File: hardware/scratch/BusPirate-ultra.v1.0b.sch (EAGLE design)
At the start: 174 parts, among them IC1 23LC1024, IC10 SN74LVC1T45DBV, IC11 SN74LVC1T45DBV, IC12 74LVC1G07DBV, IC13 SN74LVC1T45DBV, IC17 74LVC1G07DBV, IC18 SN74LVC1T45DBV, IC19 74LVC1G07DBV, IC2 23LC1024, IC20 SN74LVC1T45DBV, IC21 74LVC1G07DBV, IC22 SN74LVC1T45DBV, IC23 MCP1824_ADJ, IC24 74HCT4051, IC4 74LVC1G07DBV, IC5 74LVC1G07DBV, IC6 74LVC1G07DBV, IC7 74LVC1G07DBV, IC8 SN74LVC1T45DBV, IC9 SN74LVC1T45DBV, J2 CON_HEADER_1X04, J4 CON_HEADER_1X10-RIGHT_ANGLED_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, Q1 DMMT3906W, U1 W25X40CL, U2 STM32F103ZX, U3 ICE40HX4K, U4 MCP6001, U5 74LVC245A, U7 MCP6001, U8 74HCT4066PW, U9 74HCT4066PW

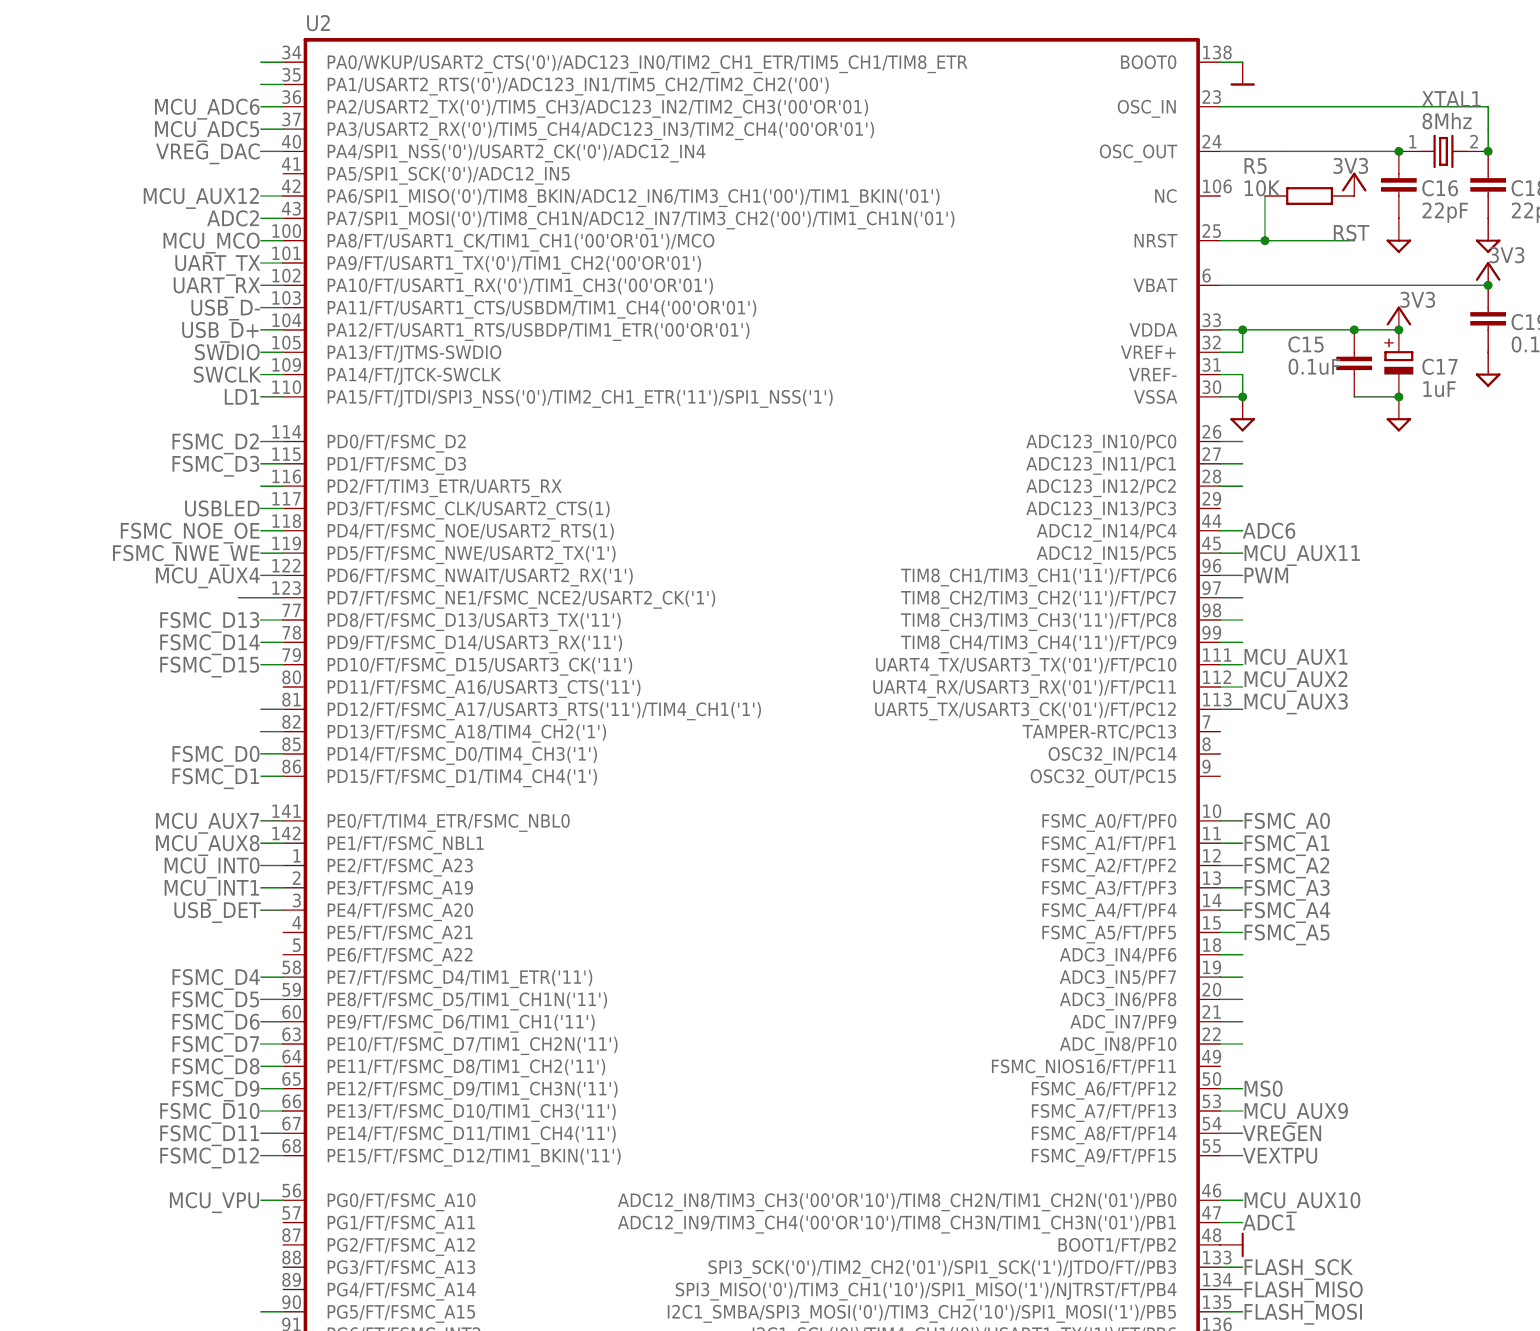
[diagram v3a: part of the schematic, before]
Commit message: move MCU_AUX12 to pin 55, reserve MCU 41-43 pins for display
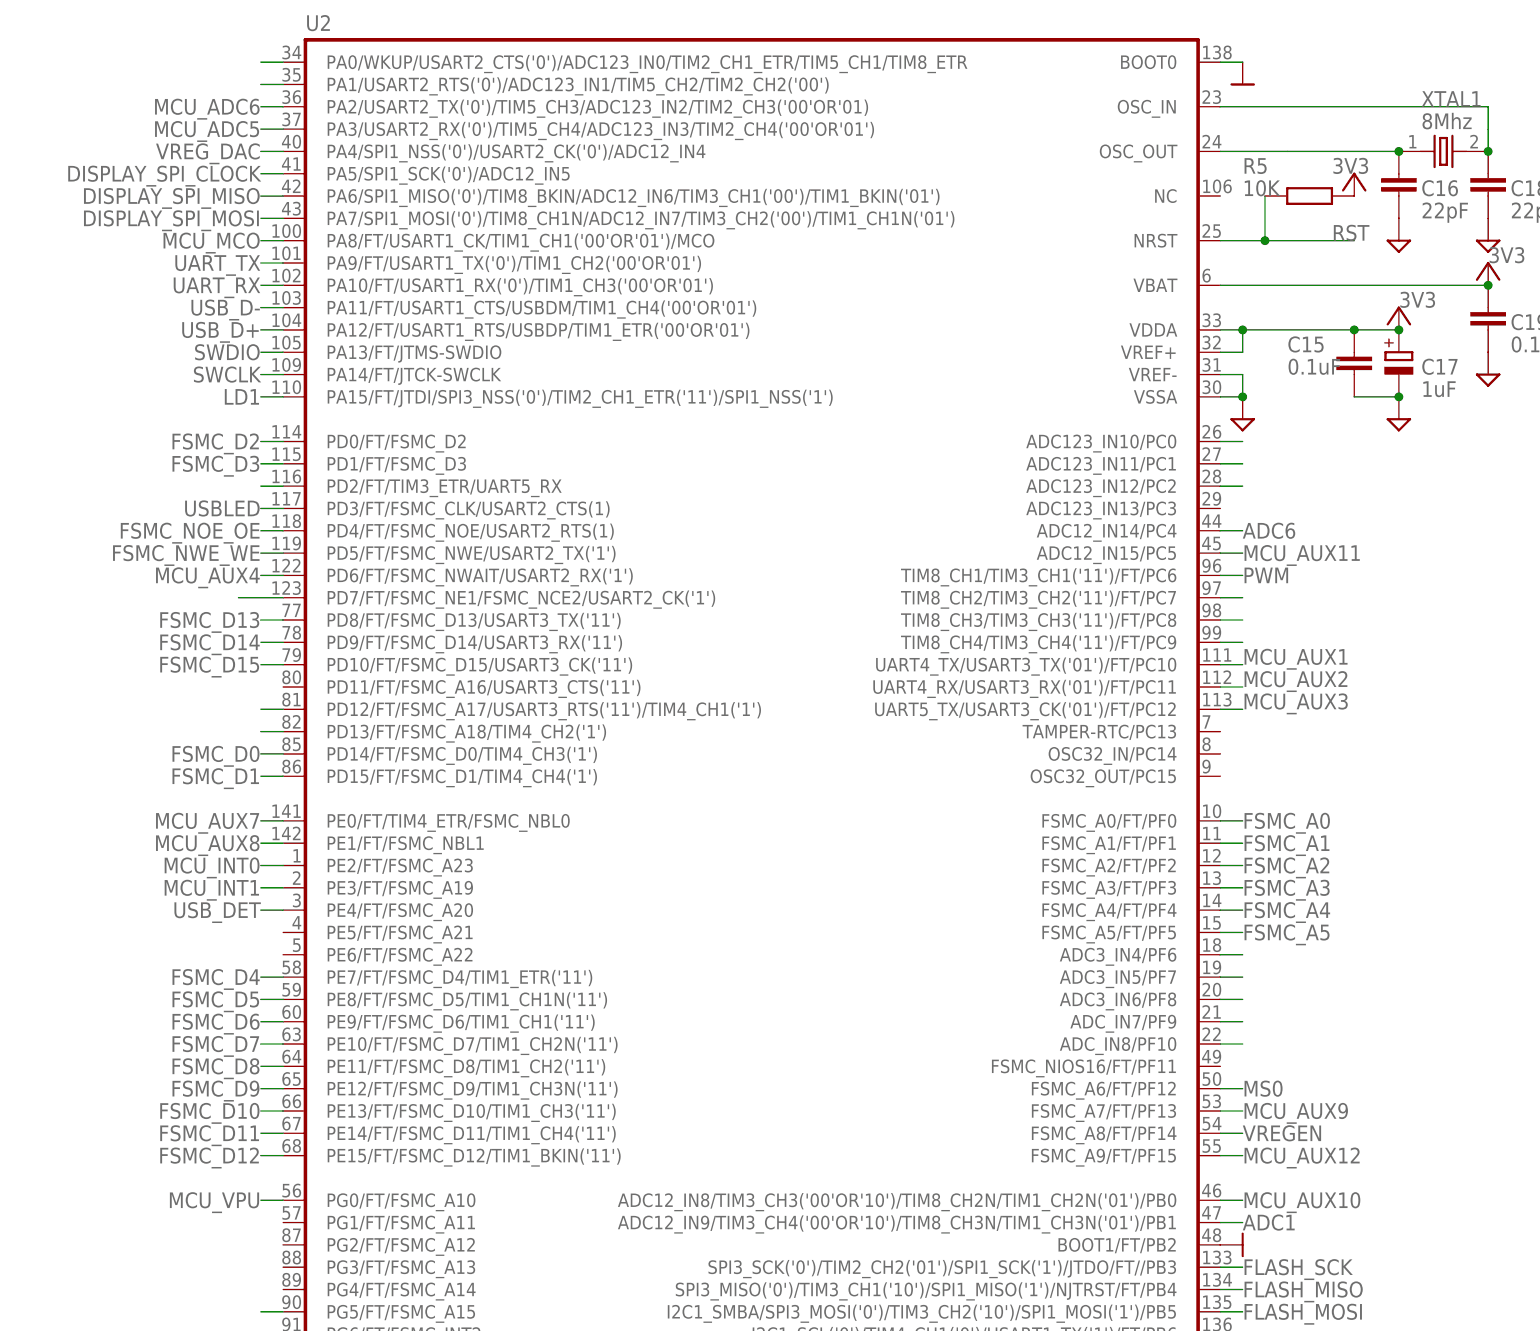
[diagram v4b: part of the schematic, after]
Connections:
- net ADC2 renamed DISPLAY_SPI_MOSI
- removed net VEXTPU: U2U.FSMC_A9/FT/PF15
- new net DISPLAY_SPI_CLOCK: U2U.PA5/SPI1_SCK('0')/ADC12_IN5
- new net DISPLAY_SPI_MISO: U2U.PA6/SPI1_MISO('0')/TIM8_BKIN/ADC12_IN6/TIM3_CH1('00')/TIM1_BKIN('01')
- net MCU_AUX12: now also U2U.FSMC_A9/FT/PF15; no longer U2U.PA6/SPI1_MISO('0')/TIM8_BKIN/ADC12_IN6/TIM3_CH1('00')/TIM1_BKIN('01')
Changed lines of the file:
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@@
-</segment>
-</net>
-<net name="ADC2" class="0">
-<segment>
-<pinref part="U2" gate="U" pin="PA7/SPI1_MOSI('0')/TIM8_CH1N/ADC12_IN7/TIM3_CH2('00')/TIM1_CH1N('01')"/>
-<wire x1="38.1" y1="411.48" x2="35.56" y2="411.48" width="0.1524" layer="91"/>
-<label x="35.56" y="411.48" size="1.778" layer="95" align="center-right"/>
 </segment>
 </net>
@@
 </segment>
 </net>
-<net name="VEXTPU" class="0">
-<segment>
-<pinref part="U2" gate="U" pin="FSMC_A9/FT/PF15"/>
-<wire x1="144.78" y1="304.8" x2="147.32" y2="304.8" width="0.1524" layer="91"/>
-<label x="147.32" y="304.8" size="1.778" layer="95" align="center-left"/>
-</segment>
-</net>
 <net name="UART_RX" class="0">
 <segment>
@@
 </segment>
 <segment>
-<pinref part="U2" gate="U" pin="PA6/SPI1_MISO('0')/TIM8_BKIN/ADC12_IN6/TIM3_CH1('00')/TIM1_BKIN('01')"/>
-<wire x1="38.1" y1="414.02" x2="35.56" y2="414.02" width="0.1524" layer="91"/>
-<label x="35.56" y="414.02" size="1.778" layer="95" align="center-right"/>
+<pinref part="U2" gate="U" pin="FSMC_A9/FT/PF15"/>
+<wire x1="144.78" y1="304.8" x2="147.32" y2="304.8" width="0.1524" layer="91"/>
+<label x="147.32" y="304.8" size="1.778" layer="95" align="center-left"/>
 </segment>
 </net>
@@
 </segment>
 </net>
+<net name="DISPLAY_SPI_CLOCK" class="0">
+<segment>
+<pinref part="U2" gate="U" pin="PA5/SPI1_SCK('0')/ADC12_IN5"/>
+<wire x1="38.1" y1="416.56" x2="35.56" y2="416.56" width="0.1524" layer="91"/>
+<label x="35.56" y="416.56" size="1.778" layer="95" align="center-right"/>
+</segment>
+</net>
+<net name="DISPLAY_SPI_MOSI" class="0">
+<segment>
+<pinref part="U2" gate="U" pin="PA7/SPI1_MOSI('0')/TIM8_CH1N/ADC12_IN7/TIM3_CH2('00')/TIM1_CH1N('01')"/>
+<wire x1="38.1" y1="411.48" x2="35.56" y2="411.48" width="0.1524" layer="91"/>
+<label x="35.56" y="411.48" size="1.778" layer="95" align="center-right"/>
+</segment>
+</net>
+<net name="DISPLAY_SPI_MISO" class="0">
+<segment>
+<pinref part="U2" gate="U" pin="PA6/SPI1_MISO('0')/TIM8_BKIN/ADC12_IN6/TIM3_CH1('00')/TIM1_BKIN('01')"/>
+<wire x1="38.1" y1="414.02" x2="35.56" y2="414.02" width="0.1524" layer="91"/>
+<label x="35.56" y="414.02" size="1.778" layer="95" align="center-right"/>
+</segment>
+</net>

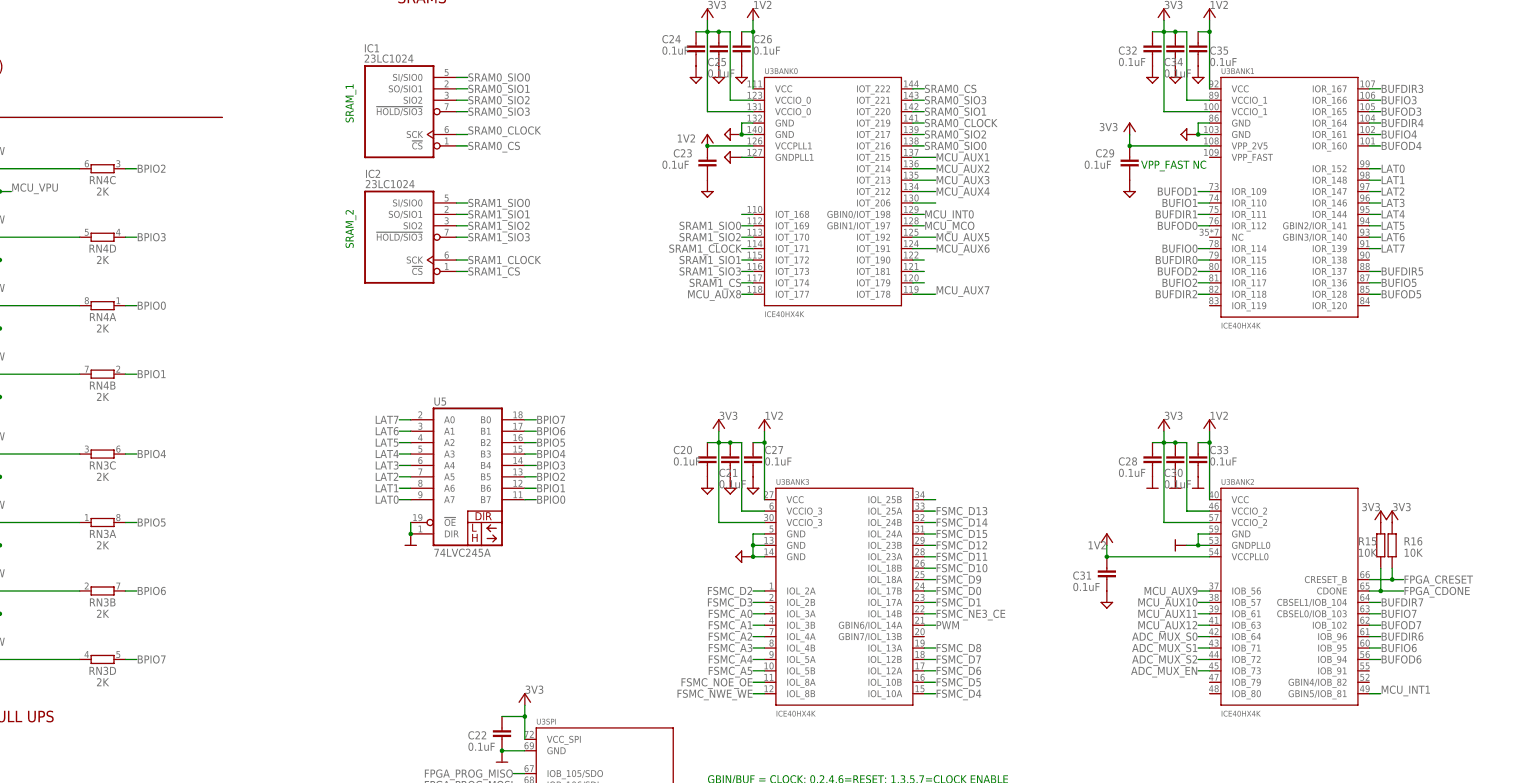
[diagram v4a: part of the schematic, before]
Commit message: changes in FPGA pin connection *BANK 1
BUFOD0 102
BUFIO0 104
BUFDIR0 101

BUFOD1 106
BUFIO1 107
BUFDIR1 105

BUFOD2 95
BUFIO2 96
BUFDIR2 94

BUFOD3 98
BUFIO3 99
BUFDIR3 97

BUFOD4 80
BUFIO4 81
BUFDIR4 82

BUFOD5 76
BUFIO5 78
BUFDIR5 79

BUFOD6 73
BUFIO6 74
BUFDIR6 75

LAT0 93
LAT1 91
LAT2 90
LAT3 88
LAT4 87
LAT5 85
LAT6 84
LAT7 83

*BANK 2

BUFOD7 62
BUFIO7 63
BUFDIR7 64

ADC_MUX_EN 61
ADC_MUX_S2 60
ADC_MUX_S1 56
ADC_MUX_S0 55
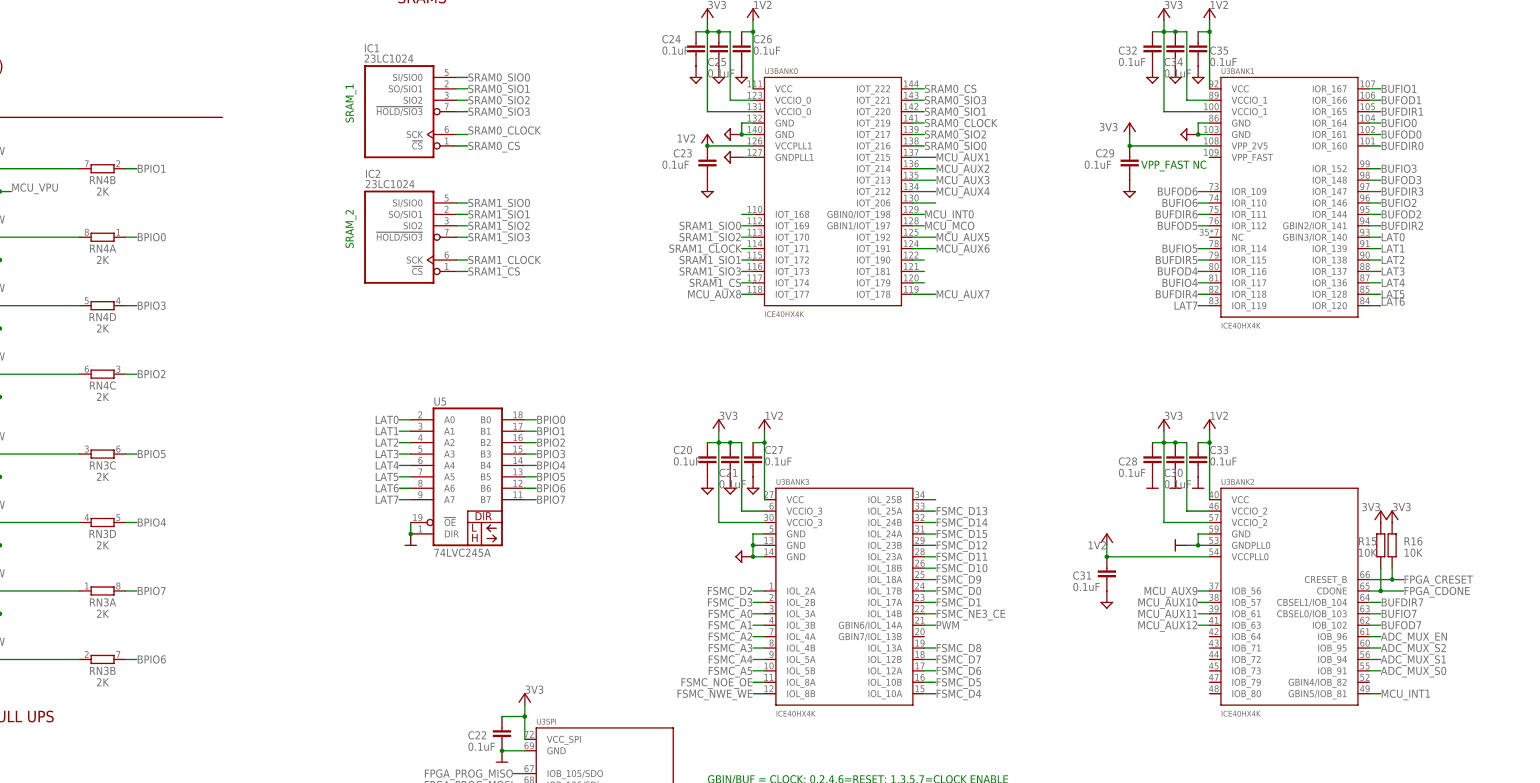
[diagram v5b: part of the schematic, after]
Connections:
- net ADC_MUX_EN: now also U3BANK2.IOB_96; no longer U3BANK2.IOB_73
- net ADC_MUX_S0: now also U3BANK2.IOB_91; no longer U3BANK2.IOB_64
- net ADC_MUX_S1: now also U3BANK2.IOB_94; no longer U3BANK2.IOB_71
- net ADC_MUX_S2: now also U3BANK2.IOB_95; no longer U3BANK2.IOB_72
- net BPIO0: now also U5G$1.B0; no longer U5G$1.B7
- net BPIO1: now also U5G$1.B1; no longer U5G$1.B6
- net BPIO2: now also U5G$1.B2; no longer U5G$1.B5
- net BPIO3: now also U5G$1.B3; no longer U5G$1.B4
- net BPIO4: now also RN3D.2, U5G$1.B4; no longer RN3C.2, U5G$1.B3
- net BPIO5: now also RN3C.2, U5G$1.B5; no longer RN3A.2, U5G$1.B2
- net BPIO6: now also U5G$1.B6; no longer U5G$1.B1
- net BPIO7: now also RN3A.2, U5G$1.B7; no longer RN3D.2, U5G$1.B0
- net BUFDIR0: now also U3BANK1.IOR_160; no longer U3BANK1.IOR_115
- net BUFDIR1: now also U3BANK1.IOR_165; no longer U3BANK1.IOR_111
- net BUFDIR2: now also U3BANK1.GBIN2/IOR_141; no longer U3BANK1.IOR_118
- net BUFDIR3: now also U3BANK1.IOR_147; no longer U3BANK1.IOR_167
- net BUFDIR4: now also U3BANK1.IOR_118; no longer U3BANK1.IOR_164
- net BUFDIR5: now also U3BANK1.IOR_115; no longer U3BANK1.IOR_137
- net BUFDIR6: now also U3BANK1.IOR_111; no longer U3BANK2.IOB_96
- net BUFIO0: now also U3BANK1.IOR_164; no longer U3BANK1.IOR_114
- net BUFIO1: now also U3BANK1.IOR_167; no longer U3BANK1.IOR_110
- net BUFIO2: now also U3BANK1.IOR_146; no longer U3BANK1.IOR_117
- net BUFIO3: now also U3BANK1.IOR_152; no longer U3BANK1.IOR_166
- net BUFIO4: now also U3BANK1.IOR_117; no longer U3BANK1.IOR_161
- net BUFIO5: now also U3BANK1.IOR_114; no longer U3BANK1.IOR_136
- net BUFIO6: now also U3BANK1.IOR_110; no longer U3BANK2.IOB_95
- net BUFOD0: now also U3BANK1.IOR_161; no longer U3BANK1.IOR_112
- net BUFOD1: now also U3BANK1.IOR_166; no longer U3BANK1.IOR_109
- net BUFOD2: now also U3BANK1.IOR_144; no longer U3BANK1.IOR_116
- net BUFOD3: now also U3BANK1.IOR_148; no longer U3BANK1.IOR_165
- net BUFOD4: now also U3BANK1.IOR_116; no longer U3BANK1.IOR_160
- net BUFOD5: now also U3BANK1.IOR_112; no longer U3BANK1.IOR_128
- net BUFOD6: now also U3BANK1.IOR_109; no longer U3BANK2.IOB_94
- net LAT0: now also U3BANK1.GBIN3/IOR_140, U5G$1.A0; no longer U3BANK1.IOR_152, U5G$1.A7
- net LAT1: now also U3BANK1.IOR_139, U5G$1.A1; no longer U3BANK1.IOR_148, U5G$1.A6
- net LAT2: now also U3BANK1.IOR_138, U5G$1.A2; no longer U3BANK1.IOR_147, U5G$1.A5
- net LAT3: now also U3BANK1.IOR_137, U5G$1.A3; no longer U3BANK1.IOR_146, U5G$1.A4
- net LAT4: now also U3BANK1.IOR_136, U5G$1.A4; no longer U3BANK1.IOR_144, U5G$1.A3
- net LAT5: now also U3BANK1.IOR_128, U5G$1.A5; no longer U3BANK1.GBIN2/IOR_141, U5G$1.A2
- net LAT6: now also U3BANK1.IOR_120, U5G$1.A6; no longer U3BANK1.GBIN3/IOR_140, U5G$1.A1
- net LAT7: now also U3BANK1.IOR_119, U5G$1.A7; no longer U3BANK1.IOR_139, U5G$1.A0
- net N$2: now also RN4B.2; no longer RN4C.2
- net N$3: now also RN4A.2; no longer RN4D.2
- net N$4: now also RN4D.2; no longer RN4A.2
- net N$42: now also RN3D.1; no longer RN3A.1
- net N$44: now also RN3A.1; no longer RN3B.1
- net N$45: now also RN3B.1; no longer RN3D.1
- net N$5: now also RN4C.2; no longer RN4B.2
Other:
- moved on the sheet: RN3A, RN3B, RN3D, RN4A, RN4B, RN4C, RN4D

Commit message: remove UART and Flash TPs, remove remaining switch, move vreg circuit
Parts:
- removed SW2: (no value), dp_devices.v6:SW_TACT_4P
- removed TP1, TP2, TP3, TP4, TP5, TP6, TP7, TP8: TPB1,27, testpad:TPB1,27
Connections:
- removed net MS0: SW2.1, SW2.2, U2U.FSMC_A6/FT/PF12
- net FLASH_CS: no longer TP7.TP
- net FLASH_MISO: no longer TP5.TP
- net FLASH_MOSI: no longer TP4.TP
- net FLASH_SCK: no longer TP6.TP
- net GND: no longer SW2.3, SW2.4, TP1.TP, TP8.TP
- net UART_RX: no longer TP2.TP
- net UART_TX: no longer TP3.TP
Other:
- note removed: "EEPROM TEST PADS"
- note removed: "NORMAL"
- note removed: "UART"
